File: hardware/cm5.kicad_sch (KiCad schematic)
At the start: 4 parts, among them J7 Conn_02x07_Odd_Even

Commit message: Small fixes
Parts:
- C22, C23: Field4 Farnell -> (none); Field5 2611911 -> (none); Field6 RM EMK105 B7104KV-F -> (none); Field7 TAIYO YUDEN EUROPE GMBH -> (none); Field8 110091611 -> (none); MPN (none) -> GRM155R71C104KA88D; Manufacturer (none) -> Murata; Mouser (none) -> https://www.mouser.com/ProductDetail/81-GRM155R71C104KA88; Mouser PN (none) -> 81-GRM155R71C104KA88; Part Description 0.1uF 10% 16V Ceramic Capacitor X7R 0402 (1005 Metric) -> (none)
- J7: Field4 Toby -> (none); Field5 THD-07-R -> (none); Field6 THD-07-R -> (none); Field7 Toby -> (none); MPN (none) -> 61301421121; Manufacturer (none) -> Wurth Elektronik; Mouser (none) -> https://www.mouser.com/ProductDetail/710-61301421121; Mouser PN (none) -> 710-61301421121; Part Description PinHeader_2x07_P2.54mm_Vertical -> (none)
- Module1: Field4 Amphenol -> (none); Field5 2x 10164227-1001A1RLF -> (none); MPN (none) -> 10164227-1001A1RLF; Manufacturer (none) -> Amphenol; Mouser (none) -> https://www.mouser.com/ProductDetail/649-01642271001A1RLF; Mouser PN (none) -> 649-01642271001A1RLF; Note (none) -> 2 pcs per board (both CM5 connectors). CM5 module (eMMC var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
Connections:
- net RP2354_SWCLK: now reaches Module1.38 (GPIO11)
- net RP2354_SWDIO: now reaches Module1.39 (GPIO8)
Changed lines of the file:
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@@
 	(wire
 		(pts
+			(xy 76.2 73.66) (xy 83.82 73.66)
+		)
+		(stroke
+			(width 0)
+			(type default)
+		)
+	)
+	(wire
+		(pts
 			(xy 251.46 104.14) (xy 254 104.14)
 		)
@@
 	(wire
 		(pts
-			(xy 147.32 81.28) (xy 147.32 68.58)
-		)
-		(stroke
-			(width 0)
-			(type solid)
-		)
-	)
-	(wire
-		(pts
 			(xy 187.96 88.9) (xy 190.5 88.9)
 		)
@@
 	(wire
 		(pts
+			(xy 147.32 68.58) (xy 147.32 81.28)
+		)
+		(stroke
+			(width 0)
+			(type solid)
+		)
+	)
+	(wire
+		(pts
 			(xy 78.74 134.62) (xy 78.74 132.08)
 		)
@@
 	(wire
 		(pts
+			(xy 144.78 76.2) (xy 152.4 76.2)
+		)
+		(stroke
+			(width 0)
+			(type default)
+		)
+	)
+	(wire
+		(pts
 			(xy 144.78 45.72) (xy 162.56 45.72)
 		)
@@
 		)
 	)
+	(hierarchical_label "RP2354_SWDIO"
+		(shape bidirectional)
+		(at 152.4 76.2 0)
+		(effects
+			(font
+				(size 1.27 1.27)
+			)
+			(justify left)
+		)
+	)
 	(hierarchical_label "USB2_P"
 		(shape bidirectional)
@@
 		)
 	)
+	(hierarchical_label "RP2354_SWCLK"
+		(shape output)
+		(at 76.2 73.66 180)
+		(effects
+			(font
+				(size 1.27 1.27)
+			)
+			(justify right)
+		)
+	)
 	(hierarchical_label "{ETH0}"
 		(shape bidirectional)
@@
 			)
 		)
-		(property "Datasheet" ""
+		(property "Datasheet" "https://cdn.amphenol-cs.com/media/wysiwyg/files/drawing/10164227.pdf"
 			(at 223.52 115.57 0)
 			(hide yes)
@@
 			)
 		)
-		(property "Description" "RaspberryPi Compute module 5"
+		(property "Description" "CONN BergStak 100P 0.4mm receptacle 1.5mm stack (CM5 socket)"
+			(at 81.28 88.9 0)
+			(hide yes)
+			(show_name no)
+			(do_not_autoplace no)
+			(effects
+				(font
+					(size 1.27 1.27)
+				)
+			)
+		)
+		(property "Manufacturer" "Amphenol"
+			(at 81.28 88.9 0)
+			(hide yes)
+			(show_name no)
+			(do_not_autoplace no)
+			(effects
+				(font
+					(size 1.27 1.27)
+				)
+			)
+		)
+		(property "MPN" "10164227-1001A1RLF"
 			(at 81.28 88.9 0)
 			(hide yes)
@@
 			)
 		)
-		(property "Field4" "Amphenol"
-			(at 220.98 20.32 0)
+		(property "Mouser PN" "649-01642271001A1RLF"
+			(at 81.28 88.9 0)
+			(hide yes)
 			(show_name no)
 			(do_not_autoplace no)
@@
 			)
 		)
-		(property "Field5" "2x 10164227-1001A1RLF"
-			(at 220.98 22.86 0)
+		(property "Mouser" "https://www.mouser.com/ProductDetail/649-01642271001A1RLF"
+			(at 81.28 88.9 0)
+			(hide yes)
+			(show_name no)
+			(do_not_autoplace no)
+			(effects
+				(font
+					(size 1.27 1.27)
+				)
+			)
+		)
+		(property "Note" "2 pcs per board (both CM5 connectors). CM5 module (eMMC variant) ordered separately."
+			(at 81.28 88.9 0)
+			(hide yes)
 			(show_name no)
 			(do_not_autoplace no)
@@
 			)
 		)
-		(property "Datasheet" "https://search.murata.co.jp/Ceramy/image/img/A01X/G101/ENG/GRM155R71C104KA88-01.pdf"
-			(at 31.75 34.29 0)
-			(hide yes)
-			(show_name no)
-			(do_not_autoplace no)
-			(effects
-				(font
-					(size 1.27 1.27)
-				)
-			)
-		)
-		(property "Description" ""
+		(property "Datasheet" "https://pim.murata.com/asset/pim4/ceramicCapacitorSMD/GRM155R71C104KA88-01A-EN_PDF_CERAMICCAPACITORSMD"
 			(at 31.75 34.29 0)
 			(hide yes)
@@
 			)
 		)
-		(property "Field4" "Farnell"
+		(property "Description" "CAP CER 100nF 16V X7R 10% 0402"
 			(at 31.75 34.29 0)
 			(hide yes)
@@
 			)
 		)
-		(property "Field5" "2611911"
+		(property "Manufacturer" "Murata"
 			(at 31.75 34.29 0)
 			(hide yes)
@@
 			)
 		)
-		(property "Field6" "RM EMK105 B7104KV-F"
+		(property "MPN" "GRM155R71C104KA88D"
 			(at 31.75 34.29 0)
 			(hide yes)
@@
 			)
 		)
-		(property "Field7" "TAIYO YUDEN EUROPE GMBH"
+		(property "Mouser PN" "81-GRM155R71C104KA88"
 			(at 31.75 34.29 0)
 			(hide yes)
@@
 			)
 		)
-		(property "Part Description" "	0.1uF 10% 16V Ceramic Capacitor X7R 0402 (1005 Metric)"
-			(at 31.75 34.29 0)
-			(hide yes)
-			(show_name no)
-			(do_not_autoplace no)
-			(effects
-				(font
-					(size 1.27 1.27)
-				)
-			)
-		)
-		(property "Field8" "110091611"
+		(property "Mouser" "https://www.mouser.com/ProductDetail/81-GRM155R71C104KA88"
 			(at 31.75 34.29 0)
 			(hide yes)
@@
 			)
 		)
-		(property "Datasheet" "https://www.toby.co.uk/uploads/publications/1673.pdf"
-			(at 30.48 72.39 0)
-			(hide yes)
-			(show_name no)
-			(do_not_autoplace no)
-			(effects
-				(font
-					(size 1.27 1.27)
-				)
-			)
-		)
-		(property "Description" ""
+		(property "Datasheet" "https://www.we-online.com/components/products/datasheet/61301421121.pdf"
 			(at 30.48 72.39 0)
 			(hide yes)
@@
 			)
 		)
-		(property "Field4" "Toby"
+		(property "Description" "CONN HDR 2x7 2.54mm vertical THT"
 			(at 30.48 72.39 0)
 			(hide yes)
@@
 			)
 		)
-		(property "Field5" "THD-07-R"
+		(property "Manufacturer" "Wurth Elektronik"
 			(at 30.48 72.39 0)
 			(hide yes)
@@
 			)
 		)
-		(property "Field6" "THD-07-R"
+		(property "MPN" "61301421121"
 			(at 30.48 72.39 0)
 			(hide yes)
@@
 			)
 		)
-		(property "Field7" "Toby"
+		(property "Mouser PN" "710-61301421121"
 			(at 30.48 72.39 0)
 			(hide yes)
@@
 			)
 		)
-		(property "Part Description" "PinHeader_2x07_P2.54mm_Vertical"
+		(property "Mouser" "https://www.mouser.com/ProductDetail/710-61301421121"
 			(at 30.48 72.39 0)
 			(hide yes)
@@
 			)
 		)
-		(property "Datasheet" ""
+		(property "Datasheet" "https://cdn.amphenol-cs.com/media/wysiwyg/files/drawing/10164227.pdf"
 			(at 259.08 110.49 0)
 			(hide yes)
@@
 			)
 		)
-		(property "Description" "RaspberryPi Compute module 5"
+		(property "Description" "CONN BergStak 100P 0.4mm receptacle 1.5mm stack (CM5 socket)"
+			(at 116.84 83.82 0)
+			(hide yes)
+			(show_name no)
+			(do_not_autoplace no)
+			(effects
+				(font
+					(size 1.27 1.27)
+				)
+			)
+		)
+		(property "Manufacturer" "Amphenol"
+			(at 116.84 83.82 0)
+			(hide yes)
+			(show_name no)
+			(do_not_autoplace no)
+			(effects
+				(font
+					(size 1.27 1.27)
+				)
+			)
+		)
+		(property "MPN" "10164227-1001A1RLF"
 			(at 116.84 83.82 0)
 			(hide yes)
@@
 			)
 		)
-		(property "Field4" "Amphenol"
-			(at 114.3 20.32 0)
+		(property "Mouser PN" "649-01642271001A1RLF"
+			(at 116.84 83.82 0)
+			(hide yes)
 			(show_name no)
 			(do_not_autoplace no)
@@
 			)
 		)
-		(property "Field5" "2x 10164227-1001A1RLF"
-			(at 114.3 22.86 0)
+		(property "Mouser" "https://www.mouser.com/ProductDetail/649-01642271001A1RLF"
+			(at 116.84 83.82 0)
+			(hide yes)
+			(show_name no)
+			(do_not_autoplace no)
+			(effects
+				(font
+					(size 1.27 1.27)
+				)
+			)
+		)
+		(property "Note" "2 pcs per board (both CM5 connectors). CM5 module (eMMC variant) ordered separately."
+			(at 116.84 83.82 0)
+			(hide yes)
 			(show_name no)
 			(do_not_autoplace no)
@@
 			)
 		)
-		(property "Datasheet" "https://search.murata.co.jp/Ceramy/image/img/A01X/G101/ENG/GRM155R71C104KA88-01.pdf"
-			(at 19.05 34.29 0)
-			(hide yes)
-			(show_name no)
-			(do_not_autoplace no)
-			(effects
-				(font
-					(size 1.27 1.27)
-				)
-			)
-		)
-		(property "Description" ""
-			(at 19.05 34.29 0)
-			(hide yes)
-			(show_name no)
-			(do_not_autoplace no)
-			(effects
-				(font
-					(size 1.27 1.27)
-				)
-			)
-		)
-		(property "Field4" "Farnell"
+		(property "Datasheet" "https://pim.murata.com/asset/pim4/ceramicCapacitorSMD/GRM155R71C104KA88-01A-EN_PDF_CERAMICCAPACITORSMD"
 			(at 19.05 34.29 0)
 			(hide yes)
@@
 			)
 		)
-		(property "Field5" "2611911"
+		(property "Description" "CAP CER 100nF 16V X7R 10% 0402"
 			(at 19.05 34.29 0)
 			(hide yes)
@@
 			)
 		)
-		(property "Field6" "RM EMK105 B7104KV-F"
+		(property "Manufacturer" "Murata"
 			(at 19.05 34.29 0)
 			(hide yes)
@@
 			)
 		)
-		(property "Field7" "TAIYO YUDEN EUROPE GMBH"
+		(property "MPN" "GRM155R71C104KA88D"
 			(at 19.05 34.29 0)
 			(hide yes)
@@
 			)
 		)
-		(property "Part Description" "	0.1uF 10% 16V Ceramic Capacitor X7R 0402 (1005 Metric)"
+		(property "Mouser PN" "81-GRM155R71C104KA88"
 			(at 19.05 34.29 0)
 			(hide yes)
@@
 			)
 		)
-		(property "Field8" "110091611"
+		(property "Mouser" "https://www.mouser.com/ProductDetail/81-GRM155R71C104KA88"
 			(at 19.05 34.29 0)
 			(hide yes)

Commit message: Add PoE circuit
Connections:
- net POE_TYP2_DET: now reaches Module1.30 (GPIO6)
- net POE_TYP3_DET: now reaches Module1.31 (GPIO12)
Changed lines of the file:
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@@
+	(wire
+		(pts
+			(xy 76.2 63.5) (xy 83.82 63.5)
+		)
+		(stroke
+			(width 0)
+			(type default)
+		)
+	)
 	(wire
 		(pts
@@
 			(width 0)
 			(type solid)
+		)
+	)
+	(wire
+		(pts
+			(xy 144.78 66.04) (xy 152.4 66.04)
+		)
+		(stroke
+			(width 0)
+			(type default)
 		)
 	)
@@
 		)
 	)
+	(hierarchical_label "POE_TYP2_DET"
+		(shape input)
+		(at 76.2 63.5 180)
+		(effects
+			(font
+				(size 1.27 1.27)
+			)
+			(justify right)
+		)
+	)
+	(hierarchical_label "POE_TYP3_DET"
+		(shape input)
+		(at 152.4 66.04 0)
+		(effects
+			(font
+				(size 1.27 1.27)
+			)
+			(justify left)
+		)
+	)

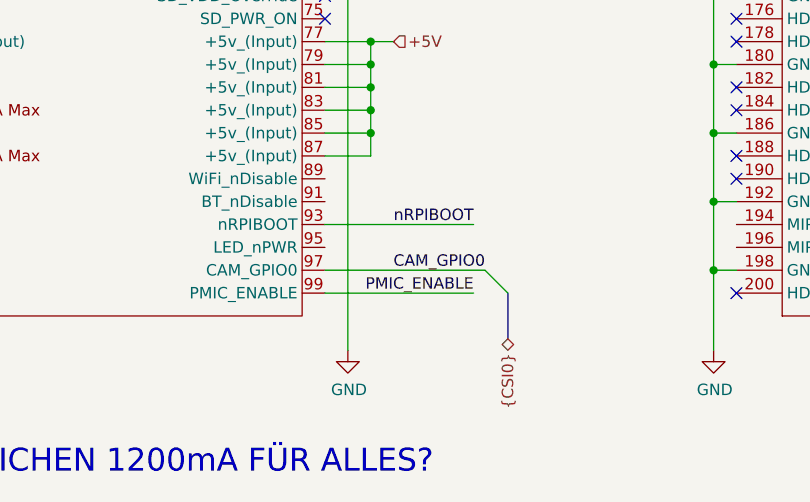
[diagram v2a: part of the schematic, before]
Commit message: Finished power management circuit
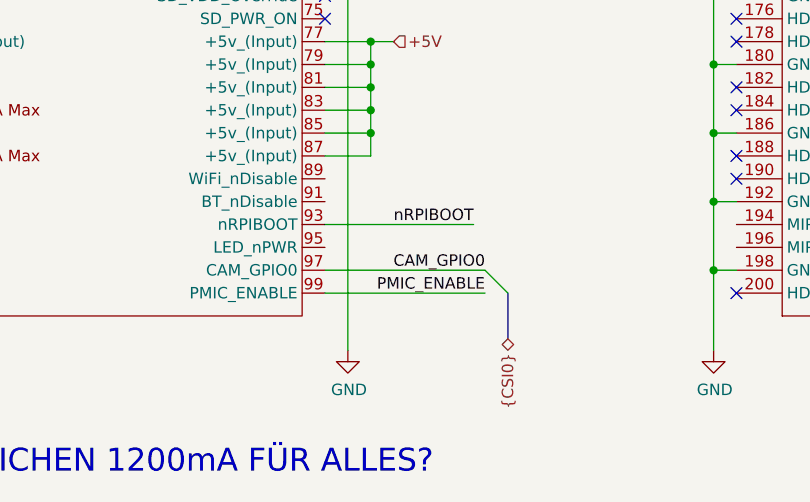
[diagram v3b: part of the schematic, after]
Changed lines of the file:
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@@
 	(wire
 		(pts
-			(xy 144.78 152.4) (xy 161.29 152.4)
+			(xy 144.78 152.4) (xy 162.56 152.4)
 		)
 		(stroke
@@
 	)
 	(label "PMIC_ENABLE"
-		(at 161.29 152.4 180)
-		(effects
-			(font
+		(at 162.56 152.4 180)
+		(effects
+			(font
